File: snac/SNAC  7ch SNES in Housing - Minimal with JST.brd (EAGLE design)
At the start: 61.3 x 64.2 mm, 32 parts, among them Q1 BSS138, Q2 BSS138, Q3 BSS138, Q4 BSS138, Q5 BSS138, Q6 BSS138, Q7 BSS138, Q8 BSS138, U1 PMIC-LDO-XC6206P332MR-G(SOT23), X1 JST-XH-09-PIN-LONG-PAD, X2 JST-XH-09-PIN-LONG-PAD

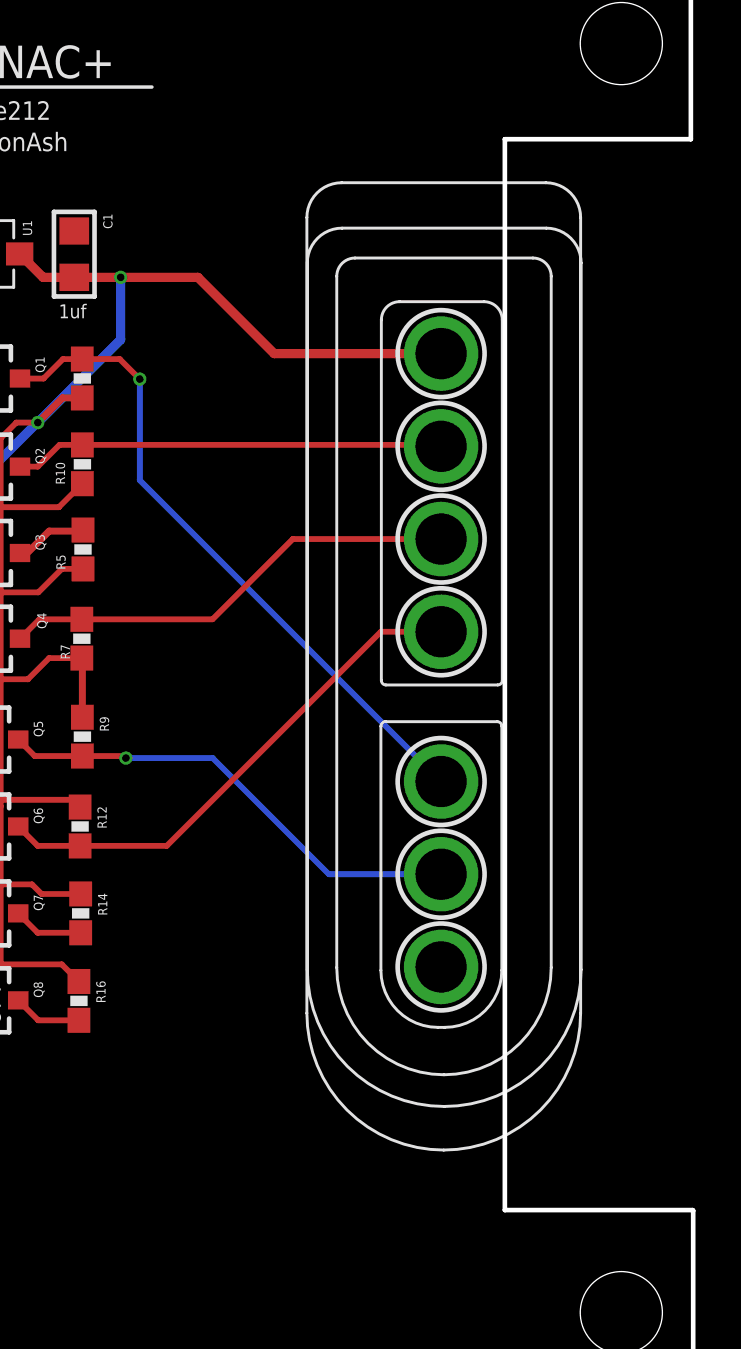
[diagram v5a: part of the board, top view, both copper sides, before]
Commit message: Moved the SNES conn on the JST version to better fit the eBay case
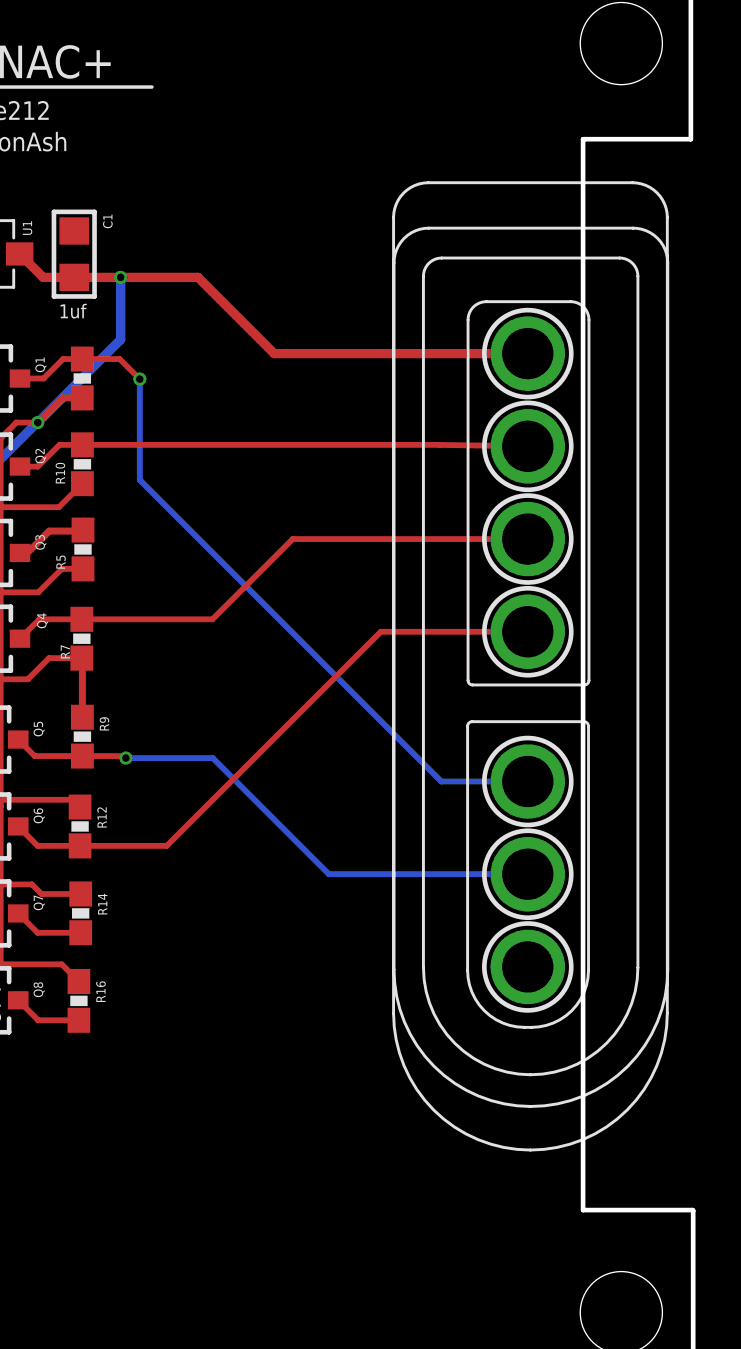
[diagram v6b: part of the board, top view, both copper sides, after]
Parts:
- moved SNES_CON 3.80 mm to (63.4, 46.9)
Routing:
- net HV6: track 22.9 -> 26.7 mm
- net HV5: track 21.0 -> 24.8 mm
- net HV4: track 20.3 -> 24.1 mm
- net HV: track 133.5 -> 137.3 mm
- net HV1: track 29.2 -> 33.0 mm
- net HV2: track 18.9 -> 22.7 mm
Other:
- outline, holes or cut-outs redrawn
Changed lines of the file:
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@@
 <wire x1="74.7014" y1="0.4572" x2="74.7014" y2="9.3472" width="0.2032" layer="20"/>
 <wire x1="74.7014" y1="9.3472" x2="74.676" y2="9.3726" width="0.2032" layer="20"/>
-<wire x1="74.676" y1="9.3726" x2="66.4464" y2="9.3726" width="0.2032" layer="20"/>
-<wire x1="66.4464" y1="9.3726" x2="66.4464" y2="56.3118" width="0.2032" layer="20"/>
-<wire x1="66.4464" y1="56.3118" x2="74.5998" y2="56.3118" width="0.2032" layer="20"/>
+<wire x1="74.676" y1="9.3726" x2="69.8754" y2="9.3726" width="0.2032" layer="20"/>
+<wire x1="69.8754" y1="9.3726" x2="69.8754" y2="56.3118" width="0.2032" layer="20"/>
+<wire x1="69.8754" y1="56.3118" x2="74.5998" y2="56.3118" width="0.2032" layer="20"/>
 <wire x1="74.5998" y1="56.3118" x2="74.5998" y2="64.6684" width="0.2032" layer="20"/>
 <wire x1="74.5998" y1="64.6684" x2="13.4112" y2="64.6684" width="0.2032" layer="20"/>
@@
 <text x="44.3484" y="17.4498" size="0.762" layer="21" font="vector" ratio="15" rot="R90">OPT</text>
 <text x="35.4076" y="46.736" size="0.6096" layer="21" font="vector" ratio="15">1uf</text>
-<dimension x1="16.2306" y1="65.3796" x2="71.7804" y2="65.4558" x3="43.99901875" y3="70.142509375" textsize="1.778" layer="1" dtype="diameter"/>
 </plain>
 <attributes>
@@
 <attribute name="VALUE" x="40.94325" y="53.18853125" size="0.889434375" layer="27" ratio="11" rot="R270"/>
 </element>
-<element name="SNES_CON" library="gamepad-conn" package="SNESCONN" value="SNESCONN" x="59.5884" y="46.9138" rot="R270"/>
+<element name="SNES_CON" library="gamepad-conn" package="SNESCONN" value="SNESCONN" x="63.3884" y="46.9138" rot="R270"/>
 <element name="X2" library="Rembrandt Electronics - JST XH Connectors v1-0" package="JST-XH-09-PACKAGE-LONG-PAD" value="JST-XH-09-PIN-LONG-PAD" x="30.4546" y="31.5976" rot="R90"/>
 <element name="C3" library="rc-master-smd" package="C0805" value="100nF" x="36.1188" y="44.3484" smashed="yes" rot="R270">
@@
 <vertex x="74.5998" y="64.6176"/>
 <vertex x="74.5998" y="56.3118"/>
-<vertex x="66.4464" y="56.3118"/>
-<vertex x="66.4464" y="9.3726"/>
+<vertex x="69.8754" y="56.3118"/>
+<vertex x="69.8754" y="9.3726"/>
 <vertex x="74.676" y="9.3726"/>
 <vertex x="74.676" y="0.4826"/>
@@
 <vertex x="74.5998" y="64.6176"/>
 <vertex x="74.5998" y="56.3118"/>
-<vertex x="66.4464" y="56.3118"/>
-<vertex x="66.4464" y="9.3726"/>
+<vertex x="69.8754" y="56.3118"/>
+<vertex x="69.8754" y="9.3726"/>
 <vertex x="74.676" y="9.3726"/>
 <vertex x="74.676" y="0.4318"/>
@@
 <wire x1="49.566459375" y1="46.674140625" x2="50.4444" y2="45.7962" width="0.254" layer="1"/>
 <via x="50.4444" y="45.7962" extent="1-16" drill="0.3302"/>
-<wire x1="50.4444" y1="45.7962" x2="50.4444" y2="41.3658" width="0.254" layer="16"/>
-<wire x1="50.4444" y1="41.3658" x2="63.6524" y2="28.1578" width="0.254" layer="16"/>
+<wire x1="50.4444" y1="45.7962" x2="50.4444" y2="41.3766" width="0.254" layer="16"/>
+<wire x1="50.4444" y1="41.3766" x2="63.6632" y2="28.1578" width="0.254" layer="16"/>
+<wire x1="63.6632" y1="28.1578" x2="67.4524" y2="28.1578" width="0.254" layer="16"/>
 </signal>
 <signal name="HV2">
@@
 <wire x1="46.9256" y1="42.9124" x2="47.9298" y2="42.9124" width="0.254" layer="1"/>
 <wire x1="47.9298" y1="42.9124" x2="63.5898" y2="42.9124" width="0.254" layer="1"/>
-<wire x1="63.5898" y1="42.9124" x2="63.6524" y2="42.8498" width="0.254" layer="1"/>
+<wire x1="63.5898" y1="42.9124" x2="67.4524" y2="42.8498" width="0.254" layer="1"/>
 </signal>
 <signal name="HV">
@@
 <wire x1="49.6062" y1="50.256440625" x2="52.994559375" y2="50.256440625" width="0.4064" layer="1"/>
 <wire x1="52.994559375" y1="50.256440625" x2="56.3372" y2="46.9138" width="0.4064" layer="1"/>
-<wire x1="56.3372" y1="46.9138" x2="63.6524" y2="46.9138" width="0.4064" layer="1"/>
+<wire x1="56.3372" y1="46.9138" x2="67.4524" y2="46.9138" width="0.4064" layer="1"/>
 <wire x1="45.974" y1="43.8912" x2="49.6062" y2="47.5234" width="0.4064" layer="16"/>
 <via x="49.6062" y="50.256440625" extent="1-16" drill="0.3302"/>
@@
 <wire x1="46.0444" y1="35.267" x2="47.9044" y2="35.267" width="0.254" layer="1"/>
 <wire x1="47.9044" y1="35.267" x2="53.6312" y2="35.267" width="0.254" layer="1"/>
-<wire x1="57.15" y1="38.7858" x2="63.6524" y2="38.7858" width="0.254" layer="1"/>
+<wire x1="57.15" y1="38.7858" x2="67.4524" y2="38.7858" width="0.254" layer="1"/>
 <wire x1="53.6312" y1="35.267" x2="57.15" y2="38.7858" width="0.254" layer="1"/>
 </signal>
@@
 <via x="49.8348" y="29.1846" extent="1-16" drill="0.3302"/>
 <wire x1="49.8348" y1="29.1846" x2="53.6448" y2="29.1846" width="0.254" layer="16"/>
-<wire x1="58.7356" y1="24.0938" x2="63.6524" y2="24.0938" width="0.254" layer="16"/>
 <wire x1="53.6448" y1="29.1846" x2="58.7356" y2="24.0938" width="0.254" layer="16"/>
+<wire x1="58.7356" y1="24.0938" x2="67.4524" y2="24.0938" width="0.254" layer="16"/>
 </signal>
 <signal name="LV6">
@@
 <wire x1="45.9682" y1="25.3374" x2="47.8282" y2="25.3374" width="0.254" layer="1"/>
 <wire x1="47.8282" y1="25.3374" x2="51.6264" y2="25.3374" width="0.254" layer="1"/>
-<wire x1="61.0108" y1="34.7218" x2="63.6524" y2="34.7218" width="0.254" layer="1"/>
+<wire x1="61.0108" y1="34.7218" x2="67.4524" y2="34.7218" width="0.254" layer="1"/>
 <wire x1="51.6264" y1="25.3374" x2="61.0108" y2="34.7218" width="0.254" layer="1"/>
 </signal>

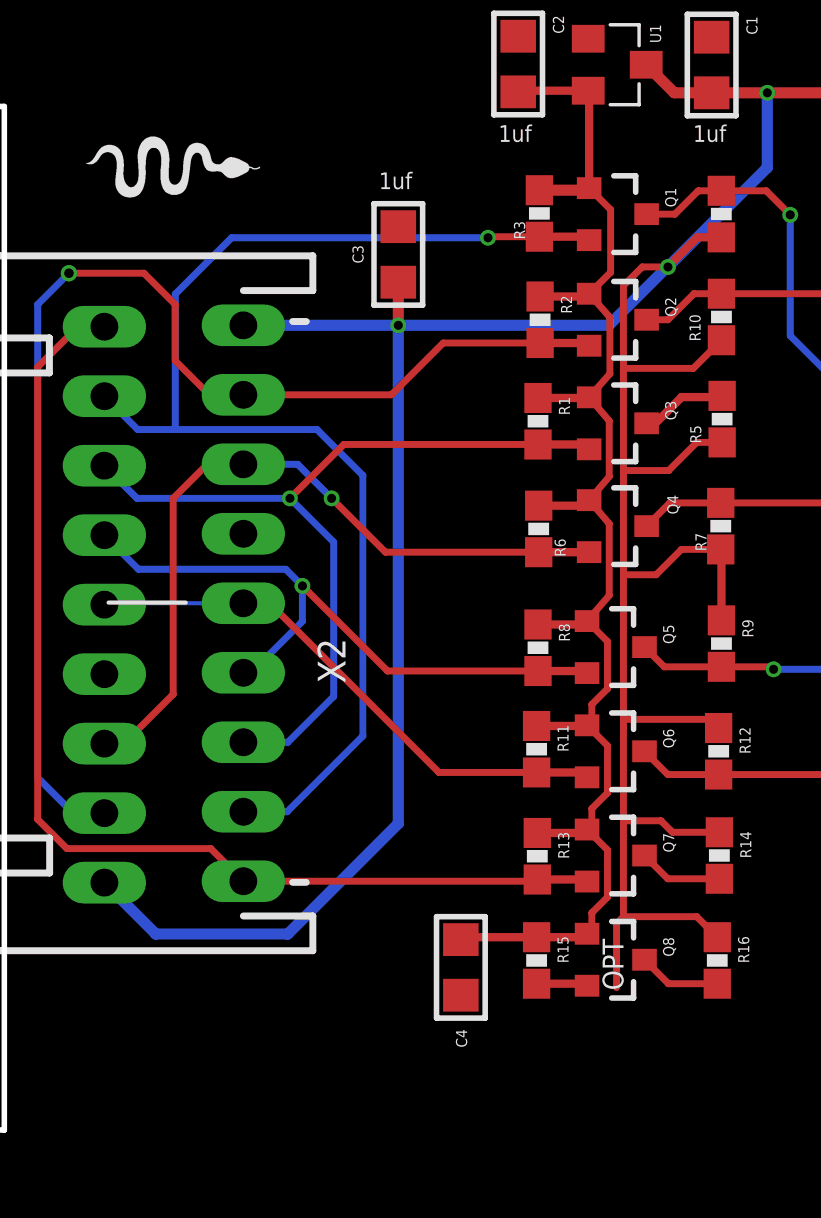
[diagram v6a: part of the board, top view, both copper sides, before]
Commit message: removed one cap from the SNES SNAC JST, as it was overkill
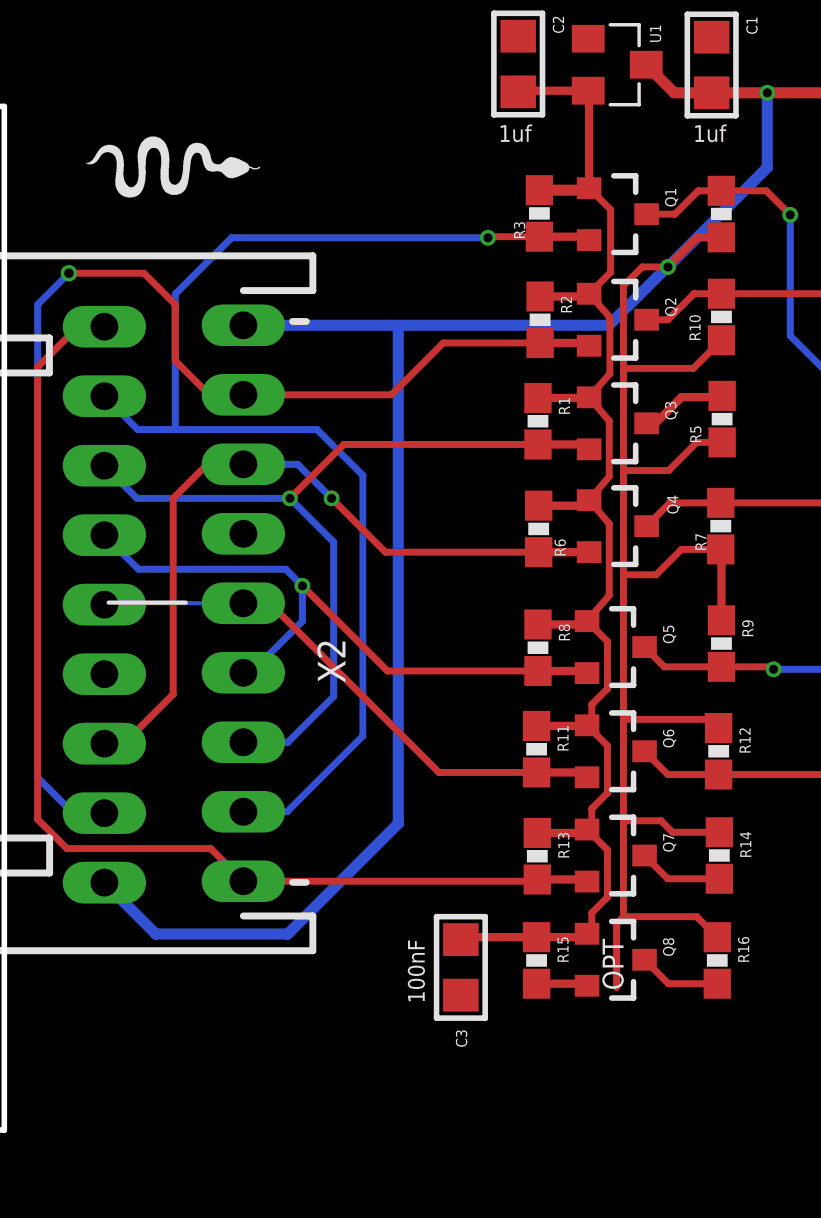
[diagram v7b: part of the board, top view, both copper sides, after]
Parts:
- removed C4: 100nF, rc-master-smd:C0805
- moved C3 26.2 mm to (38.4, 18.3), turned to 90 degrees
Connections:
- net GND: no longer C4.1
- net HV: no longer C3.2
- net LV: now also C3.2; no longer C4.2
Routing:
- net HV: track 137.3 -> 135.7 mm, vias 3 -> 2
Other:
- board text added: "100nF"
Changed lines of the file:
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@@
 <text x="41.3258" y="55.788559375" size="0.8128" layer="21" ratio="15">ElectronAsh</text>
 <text x="44.3484" y="17.4498" size="0.762" layer="21" font="vector" ratio="15" rot="R90">OPT</text>
-<text x="35.4076" y="46.736" size="0.6096" layer="21" font="vector" ratio="15">1uf</text>
+<text x="37.084" y="16.9672" size="0.6096" layer="21" font="vector" ratio="15" rot="R90">100nF</text>
 </plain>
 <attributes>
@@
 <element name="SNES_CON" library="gamepad-conn" package="SNESCONN" value="SNESCONN" x="63.3884" y="46.9138" rot="R270"/>
 <element name="X2" library="Rembrandt Electronics - JST XH Connectors v1-0" package="JST-XH-09-PACKAGE-LONG-PAD" value="JST-XH-09-PIN-LONG-PAD" x="30.4546" y="31.5976" rot="R90"/>
-<element name="C3" library="rc-master-smd" package="C0805" value="100nF" x="36.1188" y="44.3484" smashed="yes" rot="R270">
-<attribute name="NAME" x="34.8488" y="44.0182" size="0.4064" layer="25" ratio="18" rot="R90"/>
-<attribute name="VALUE" x="34.3408" y="46.1264" size="0.4064" layer="27" ratio="10" rot="R270"/>
-</element>
-<element name="C4" library="rc-master-smd" package="C0805" value="100nF" x="38.4048" y="18.288" smashed="yes" rot="R90">
+<element name="C3" library="rc-master-smd" package="C0805" value="100nF" x="38.4048" y="18.288" smashed="yes" rot="R90">
 <attribute name="NAME" x="38.227" y="16.0274" size="0.4064" layer="25" ratio="18" rot="R270"/>
 <attribute name="VALUE" x="40.1828" y="16.51" size="0.4064" layer="27" ratio="10" rot="R90"/>
@@
 <contactref element="X2" pad="4"/>
 <contactref element="C3" pad="1"/>
-<contactref element="C4" pad="1"/>
 <contactref element="X1" pad="4"/>
 </signal>
@@
 <wire x1="42.9768" y1="50.3326" x2="40.54090625" y2="50.3326" width="0.3048" layer="1"/>
 <wire x1="40.54090625" y1="50.3326" x2="40.50030625" y2="50.292" width="0.3048" layer="1"/>
-<contactref element="C4" pad="2"/>
+<contactref element="C3" pad="2"/>
 <wire x1="40.2336" y1="50.292" x2="40.50030625" y2="50.292" width="0.3048" layer="1"/>
 <contactref element="R6" pad="1"/>
@@
 <wire x1="46.205959375" y1="50.256440625" x2="47.571659375" y2="50.256440625" width="0.4064" layer="1"/>
 <wire x1="45.0342" y1="51.137" x2="45.1798" y2="51.2826" width="0.4064" layer="1"/>
-<contactref element="C3" pad="2"/>
 <contactref element="SNES_CON" pad="5V"/>
 <wire x1="30.4546" y1="41.7576" x2="36.1188" y2="41.7576" width="0.4064" layer="16"/>
@@
 <wire x1="47.9298" y1="41.2124" x2="46.9002" y2="40.1828" width="0.254" layer="1"/>
 <wire x1="46.9002" y1="40.1828" x2="44.3484" y2="40.1828" width="0.254" layer="1"/>
-<via x="36.1188" y="41.7576" extent="1-16" drill="0.3302"/>
-<wire x1="36.1188" y1="41.7576" x2="36.1188" y2="43.3324" width="0.4064" layer="1"/>
 <wire x1="36.1188" y1="41.7576" x2="43.815" y2="41.7576" width="0.4064" layer="16"/>
 <wire x1="43.815" y1="41.7576" x2="45.9486" y2="43.8912" width="0.4064" layer="16"/>
